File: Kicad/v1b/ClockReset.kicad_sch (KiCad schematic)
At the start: 20 parts, among them SW1 RESET, U2 74HC14, U3 74HC4520, U4 74HC4040, U5 SST39SF, U6 74HC574, Y1 12 Mhz

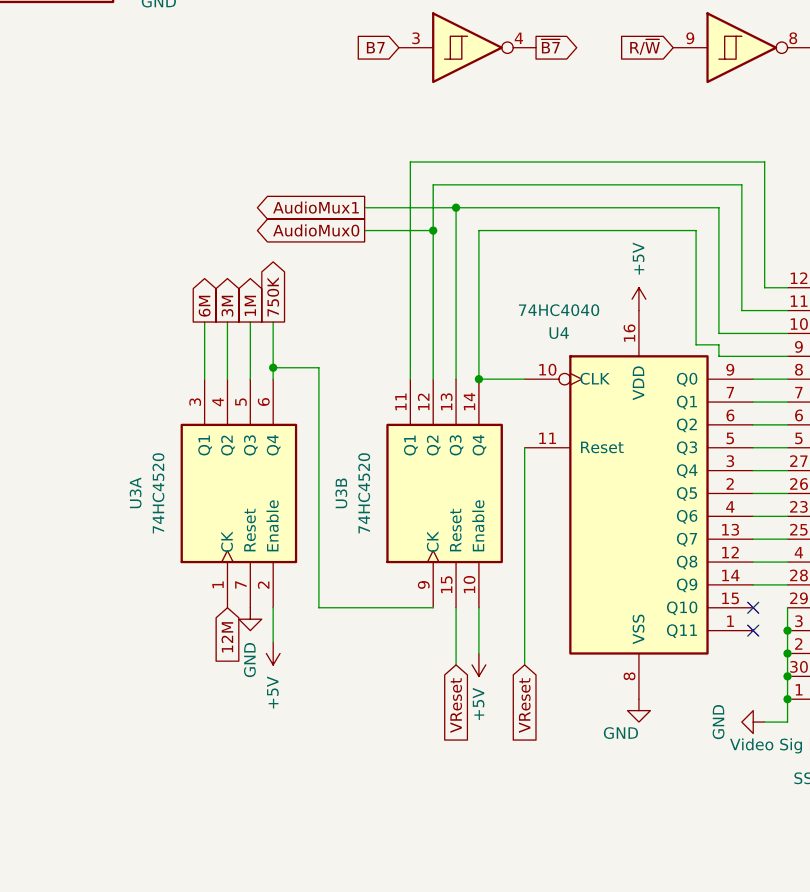
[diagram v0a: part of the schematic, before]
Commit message: Video ROM update, cart files, v1b main board
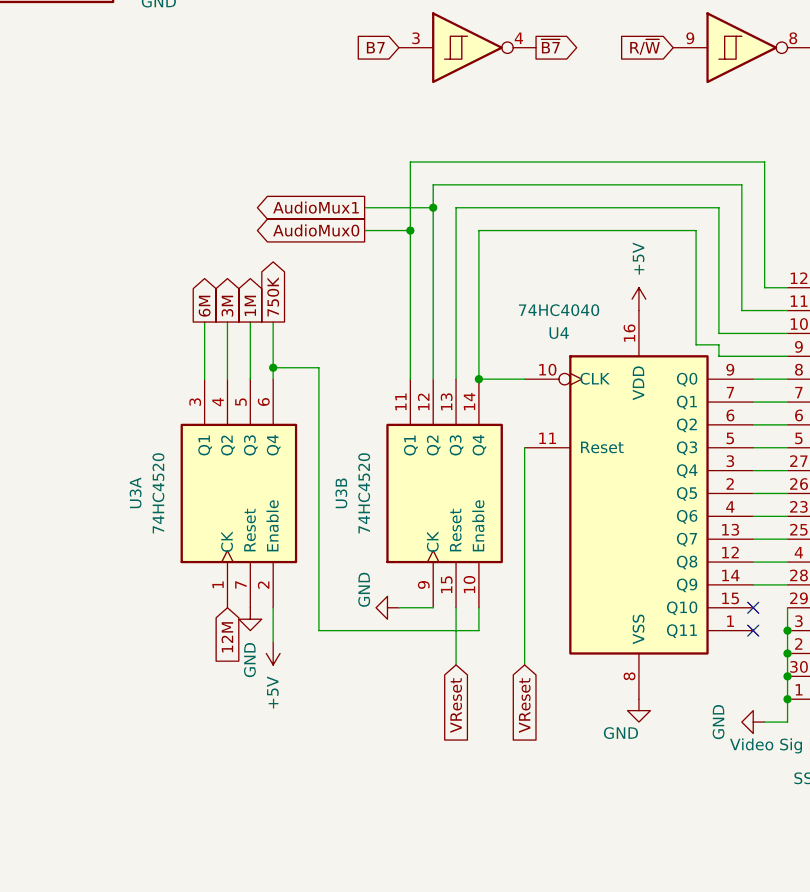
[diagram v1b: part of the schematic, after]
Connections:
- net +5V: no longer U3.10 (Enable)
- net 750K: now also U3.10 (Enable); no longer U3.9 (CK)
- net AudioMux0: now also U3.11 (Q1), U5.12 (A0); no longer U3.12 (Q2), U5.11 (A1)
- net AudioMux1: now also U3.12 (Q2), U5.11 (A1); no longer U3.13 (Q3), U5.10 (A2)
- net GND: now also U3.9 (CK)
- new net: U3.13 (Q3), U5.10 (A2)
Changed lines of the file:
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@@
   (junction (at 114.3 124.46) (diameter 0) (color 0 0 0 0)
   )
-  (junction (at 74.93 80.01) (diameter 0) (color 0 0 0 0)
-  )
   (junction (at 113.03 182.88) (diameter 0) (color 0 0 0 0)
   )
@@
   (junction (at 134.62 127) (diameter 0) (color 0 0 0 0)
   )
+  (junction (at 74.93 77.47) (diameter 0) (color 0 0 0 0)
+  )
   (junction (at 177.8 58.42) (diameter 0) (color 0 0 0 0)
   )
   (junction (at 100.33 175.26) (diameter 0) (color 0 0 0 0)
   )
-  (junction (at 77.47 77.47) (diameter 0) (color 0 0 0 0)
-  )
   (junction (at 157.48 58.42) (diameter 0) (color 0 0 0 0)
+  )
+  (junction (at 72.39 80.01) (diameter 0) (color 0 0 0 0)
   )
   (junction (at 125.73 175.26) (diameter 0) (color 0 0 0 0)
@@
     (stroke (width 0) (type default))
   )
-  (wire (pts (xy 67.31 80.01) (xy 74.93 80.01))
-    (stroke (width 0) (type default))
-  )
   (wire (pts (xy 77.47 128.27) (xy 77.47 121.92))
     (stroke (width 0) (type default))
@@
     (stroke (width 0) (type default))
   )
-  (wire (pts (xy 67.31 77.47) (xy 77.47 77.47))
-    (stroke (width 0) (type default))
-  )
   (wire (pts (xy 114.3 99.06) (xy 110.49 99.06))
     (stroke (width 0) (type default))
@@
     (stroke (width 0) (type default))
   )
+  (wire (pts (xy 72.39 80.01) (xy 72.39 96.52))
+    (stroke (width 0) (type default))
+  )
   (wire (pts (xy 72.39 72.39) (xy 111.76 72.39))
     (stroke (width 0) (type default))
   )
-  (wire (pts (xy 74.93 74.93) (xy 74.93 80.01))
-    (stroke (width 0) (type default))
-  )
   (wire (pts (xy 114.3 96.52) (xy 110.49 96.52))
     (stroke (width 0) (type default))
@@
     (stroke (width 0) (type default))
   )
+  (wire (pts (xy 74.93 77.47) (xy 74.93 96.52))
+    (stroke (width 0) (type default))
+  )
   (wire (pts (xy 85.09 128.27) (xy 85.09 104.14))
     (stroke (width 0) (type default))
@@
     (stroke (width 0) (type default))
   )
-  (wire (pts (xy 80.01 127) (xy 80.01 121.92))
-    (stroke (width 0) (type default))
-  )
   (wire (pts (xy 177.8 44.45) (xy 177.8 58.42))
     (stroke (width 0) (type default))
@@
     (stroke (width 0) (type default))
   )
-  (wire (pts (xy 72.39 72.39) (xy 72.39 96.52))
+  (wire (pts (xy 72.39 72.39) (xy 72.39 80.01))
+    (stroke (width 0) (type default))
+  )
+  (wire (pts (xy 80.01 124.46) (xy 80.01 121.92))
+    (stroke (width 0) (type default))
+  )
+  (wire (pts (xy 67.31 80.01) (xy 72.39 80.01))
     (stroke (width 0) (type default))
   )
@@
     (stroke (width 0) (type default))
   )
+  (wire (pts (xy 71.12 121.92) (xy 74.93 121.92))
+    (stroke (width 0) (type default))
+  )
   (wire (pts (xy 125.73 175.26) (xy 138.43 175.26))
     (stroke (width 0) (type default))
@@
     (stroke (width 0) (type default))
   )
-  (wire (pts (xy 74.93 121.92) (xy 62.23 121.92))
+  (wire (pts (xy 62.23 124.46) (xy 80.01 124.46))
     (stroke (width 0) (type default))
   )
@@
     (stroke (width 0) (type default))
   )
-  (wire (pts (xy 74.93 80.01) (xy 74.93 96.52))
+  (wire (pts (xy 67.31 77.47) (xy 74.93 77.47))
+    (stroke (width 0) (type default))
+  )
+  (wire (pts (xy 74.93 74.93) (xy 74.93 77.47))
     (stroke (width 0) (type default))
   )
@@
     (stroke (width 0) (type default))
   )
-  (wire (pts (xy 62.23 121.92) (xy 62.23 95.25))
+  (wire (pts (xy 62.23 124.46) (xy 62.23 95.25))
     (stroke (width 0) (type default))
   )
@@
     )
   )
+  (symbol (lib_id "power:GND") (at 71.12 121.92 270) (unit 1)
+    (in_bom yes) (on_board yes) (dnp no)
+    (property "Reference" "#PWR017" (at 64.77 121.92 0)
+      (effects (font (size 1.27 1.27)) hide)
+    )
+    (property "Value" "GND" (at 67.31 121.92 0)
+      (effects (font (size 1.27 1.27)) (justify right))
+    )
+    (property "Footprint" "" (at 71.12 121.92 0)
+      (effects (font (size 1.27 1.27)) hide)
+    )
+    (property "Datasheet" "" (at 71.12 121.92 0)
+      (effects (font (size 1.27 1.27)) hide)
+    )
+    (pin "1")
+    (instances
+      (project "v1b"
+        (path "/82bc3382-6295-4121-a2db-2433a00f189b/470e69f3-fa8a-41f9-93cf-a95a9c1e6a1d"
+          (reference "#PWR017") (unit 1)
+        )
+      )
+    )
+  )
   (symbol (lib_id "Device:C") (at 151.13 179.07 0) (unit 1)
     (in_bom yes) (on_board yes) (dnp no) (fields_autoplaced)
@@
         )
       )
-    )
-  )
-  (symbol (lib_id "power:+5V") (at 80.01 127 180) (unit 1)
-    (in_bom yes) (on_board yes) (dnp no) (fields_autoplaced)
-    (property "Reference" "#PWR017" (at 80.01 123.19 0)
-      (effects (font (size 1.27 1.27)) hide)
-    )
-    (property "Value" "+5V" (at 80.01 130.81 90)
-      (effects (font (size 1.27 1.27)) (justify left))
-    )
-    (property "Footprint" "" (at 80.01 127 0)
-      (effects (font (size 1.27 1.27)) hide)
-    )
-    (property "Datasheet" "" (at 80.01 127 0)
-      (effects (font (size 1.27 1.27)) hide)
-    )
-    (pin "1")
-    (instances
-      (project "v1b"
-        (path "/82bc3382-6295-4121-a2db-2433a00f189b/470e69f3-fa8a-41f9-93cf-a95a9c1e6a1d"
-          (reference "#PWR017") (unit 1)
-        )
-      )
